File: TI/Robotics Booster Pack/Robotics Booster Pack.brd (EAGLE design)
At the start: 68.6 x 76.2 mm, 119 parts, among them U1 DRV8800, U10 74LVTH125.RGY, U11 SCHA4B0400, U12 BLUETOOTH-RN41", U13 XBEE-1XBEE-1_LOCK, U14 FDMA1024NZ, U2 DRV8800, U3 DRV8800, U4 DRV8800, U5 TPS5331[8/9].DQP, U6 TPS62082.DSG, U7 PCA9557.RGV, U8 MPU-6050, U9 INA220.DGS

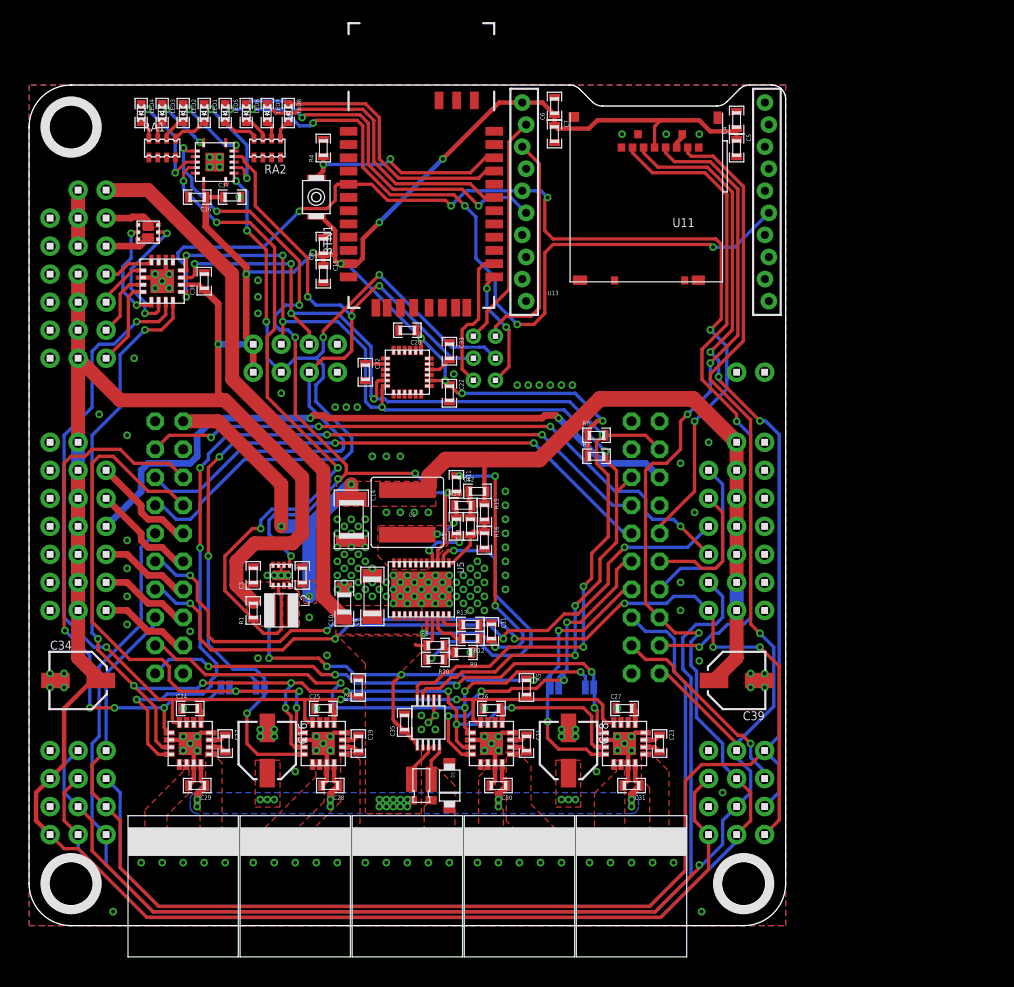
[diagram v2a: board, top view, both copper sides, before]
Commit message: Addressed all issues in github repo Moved GPIO & Mosfet connections up because of USB connector in Launchpad Fixed SPI pin swap Added diode between 5v and VBUS Changed jumpers for UART BT/XBee selection to SMD Jumpers
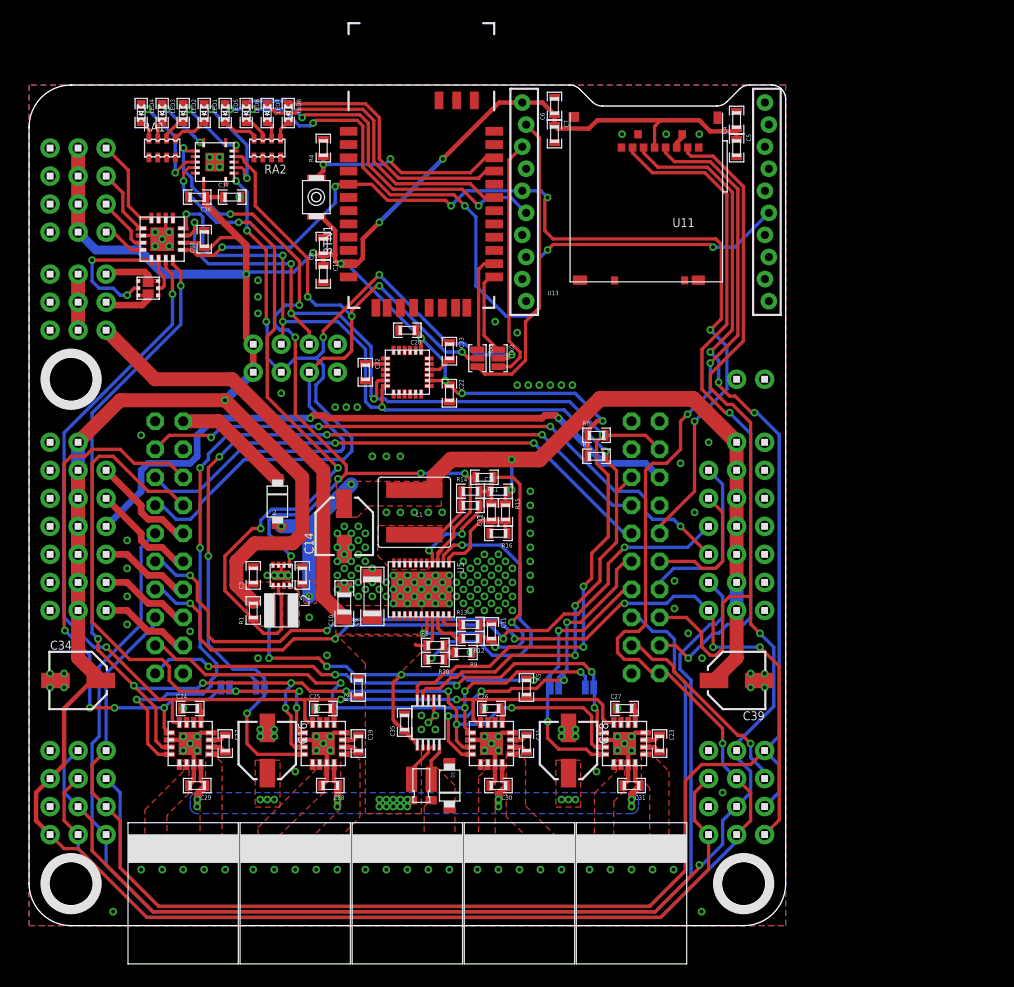
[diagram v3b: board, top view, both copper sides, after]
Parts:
- removed H23: 2X3, headers(2mm):2X3
- removed H27: 1X2, headers(.1in):1X2
- added D2: (no value), nxp:SOD123W
- added RXI, TXO: (no value), solderjumper:3.LRG
- C14: device standardparts:1210 -> microbuilder:PANASONIC_C
- C16, C18: value 100uF -> 47uF
- H7, H8, H9: value 1X2 -> 1X3; device headers(.1in):1X2 -> headers(.1in):1X3
- U14: value FDMA1024NZ -> FDMA3028N
- moved U$11 22.9 mm to (3.81, 49.5)
- moved H10 19.0 mm to (1.91, 70.5), turned to 270 degrees
- moved H11 19.0 mm to (4.45, 70.5), turned to 270 degrees
- moved H12 11.4 mm to (6.99, 70.5)
- moved H8 7.62 mm to (4.45, 54.0)
- moved H9 5.08 mm to (6.99, 59.1)
- moved U14 5.08 mm to (10.8, 57.8)
- moved C38 3.81 mm to (15.9, 62.2)
- moved U7 3.81 mm to (12.1, 62.2)
- moved R11 2.62 mm to (41.3, 40.6), turned to 180 degrees
- moved H7 2.54 mm to (1.91, 59.1), turned to 270 degrees
- moved C1 2.29 mm to (40.0, 38.1), turned to 180 degrees
- moved C13 2.29 mm to (41.9, 37.5)
- moved C12 1.91 mm to (42.5, 39.4)
- moved R15 1.91 mm to (43.2, 37.5)
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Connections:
- new net N$16: D2.P$2, U$8.VBUS
- net 5.0V: now also C14.+, D2.P$1; no longer C14.1, U$8.VBUS
- net BT.RXI: now also RXI.1; no longer H23.5
- net BT.TXO: now also TXO.1; no longer H23.6
- net GND: now also C14.-, H7.3; no longer C14.2
- net SPI.MISO: now also U$8.PA4; no longer U$8.PA2
- net SPI.SCLK: now also U$8.PA2; no longer U$8.PA4
- net UART.RXI: now also RXI.2; no longer H23.3
- net UART.TXO: now also TXO.2; no longer H23.4
- net VBAT: now also H9.3; no longer H27.2
- net VIN: now also H8.3; no longer H27.1
- net XBEE.RXI: now also RXI.3; no longer H23.1
- net XBEE.TXO: now also TXO.3; no longer H23.2
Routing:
- net 5.0V: track 90.8 -> 74.8 mm, vias 3 -> 5
- net VBAT: track 75.5 -> 64.4 mm
- net N$16: track 0.00 -> 10.8 mm
- net FET1.G: track 12.1 -> 3.17 mm, vias 2 -> 0
- net XBEE.RXI: track 21.2 -> 27.5 mm
- net !RST: track 93.8 -> 87.8 mm
- net SPI.MISO: track 156.1 -> 161.1 mm
- net BT.RXI: track 13.0 -> 8.97 mm
- net IO0: track 4.63 -> 8.62 mm
- net IO3: track 7.75 -> 3.85 mm
- net M.EN: track 108.2 -> 111.7 mm
- net 5V.PG: track 72.9 -> 76.3 mm
- net BT.TXO: track 11.0 -> 7.73 mm, vias 2 -> 0
- net I2C.SDA: track 95.4 -> 98.5 mm
- net N$2: track 5.09 -> 8.11 mm
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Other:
- board text added: "!CS!"
- board text added: "VBATT"
- board text removed: "CS"

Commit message: Created AS5035 FLoating Encoder
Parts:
- moved H6 12.7 mm to (6.99, 41.3), turned to 270 degrees
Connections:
- net AD0: now also H6.6; no longer H6.1
- net AD1: now also H6.5; no longer H6.2
- net AD2: now also H6.4; no longer H6.3
- net AD3: now also H6.3; no longer H6.4
- net AD4: now also H6.2; no longer H6.5
- net AD5: now also H6.1; no longer H6.6

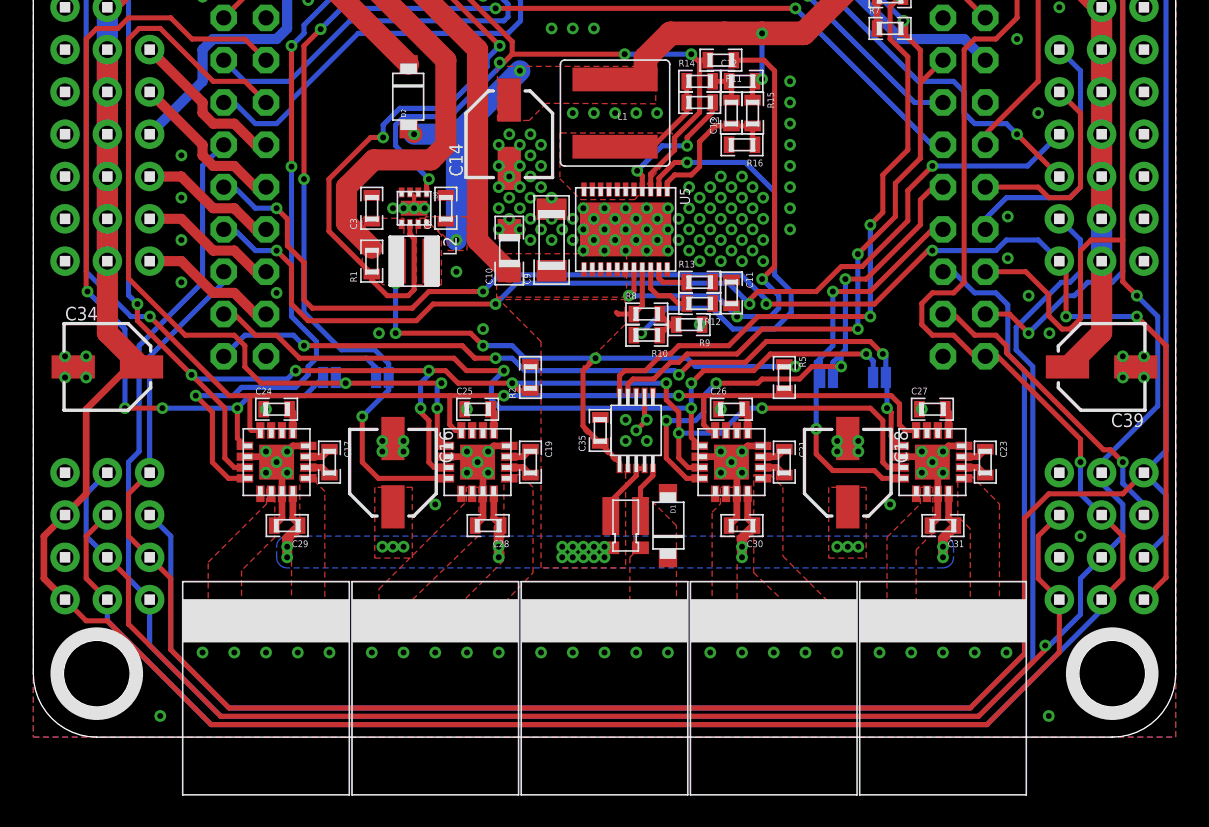
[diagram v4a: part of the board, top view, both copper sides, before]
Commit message: Changed Pinouts of BoosterPack * SPI Encoders replaced with QEI * SD Card/SPI interface moved to port F * Motor Control Signals moved to port A
Layout still needs to be redone...
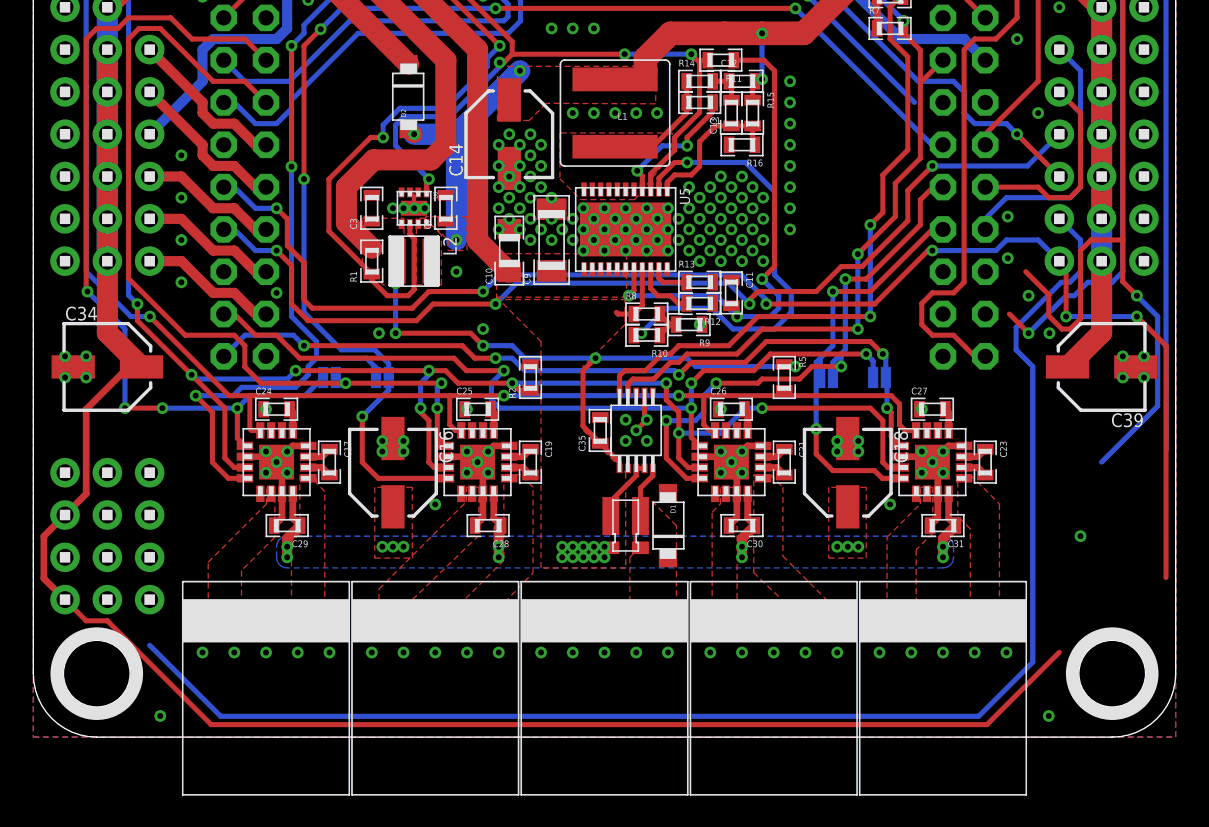
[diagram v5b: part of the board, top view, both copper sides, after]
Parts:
- removed H15, H16: 2X3, headers(.1in):2X3
- moved H14 59.9 mm to (1.91, 8.26)
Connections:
- removed net ENC0.!CS: H13.5, U$8.PD6
- removed net ENC1.!CS: H14.5, U$8.PD7
- removed net SPI.FSS: U$8.PA3, U11.!CS!/NC/DAT3
- new net QEI0.A: U$8.PD6
- new net QEI0.B: U$8.PD7
- new net QEI1.A: U$8.PC5
- new net QEI1.B: U$8.PC6
- new net SPI*.!CS: U$8.PC7
- new net SPI.!CS: U$8.PC4, U11.!CS!/NC/DAT3
- new net UART*.RXI: U$8.PE5
- new net UART*.TXO: U$8.PE4
- net 3.3V: no longer H15.1, H16.1
- net GND: no longer H15.2, H16.2
- net M0.DIR: now also U$8.PA2; no longer U$8.PC4
- net M1.DIR: now also U$8.PA3; no longer U$8.PC5
- net M2.DIR: now also U$8.PA4; no longer U$8.PC6
- net M3.DIR: now also U$8.PA5; no longer U$8.PC7
- net SPI.MISO: now also U$8.PF0; no longer H13.4, H14.4, H15.4, H16.4, U$8.PA4
- net SPI.MOSI: now also U$8.PF1; no longer H13.6, H14.6, H15.6, H16.6, U$8.PA5
- net SPI.SCLK: now also U$8.PF2; no longer H13.3, H14.3, H15.3, H16.3, U$8.PA2
- net SVRO4/ENC2.!CS: no longer H15.5, U$8.PE4
- net SVRO5/ENC3.!CS: no longer H16.5, U$8.PE5
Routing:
- net SPI.MOSI: track 168.0 -> 63.3 mm
- net SPI.SCLK: track 153.1 -> 60.4 mm, vias 3 -> 2
- net ENC0.!CS: track 88.7 -> 0.00 mm
- net SPI.MISO: track 161.1 -> 75.2 mm, vias 2 -> 1
- net SPI.FSS: track 62.2 -> 0.00 mm, vias 2 -> 0
- net SPI.!CS: track 0.00 -> 60.7 mm, vias 0 -> 2
- net SVRO4/ENC2.!CS: track 118.5 -> 85.6 mm
- net ENC1.!CS: track 18.4 -> 0.00 mm, vias 1 -> 0
- net 3.3V: track 363.2 -> 353.9 mm
- net SVRO5/ENC3.!CS: track 85.3 -> 82.8 mm
- net M0.DIR: track 82.3 -> 80.6 mm
- net M1.DIR: track 77.0 -> 76.4 mm
- net M3.DIR: track 25.2 -> 24.5 mm
- net M2.DIR: track 33.2 -> 32.6 mm

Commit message: Started routing v2. And by started, I mean rerouting _everything_
... The heck's wrong with me ...
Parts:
- removed BTN1: B3U-1000P(M)-B, omron:B3U-1000P(M)-B
- removed U$6, U$7: 1X4, headers(.1in):1X4
- added J2: (no value), solderjumper:2.MED
- added U$14: HOLE.4MM, screw_holes:4MM
- added U$9: 2X4, headers(.1in):2X4
- C14, C16, C18, C34, C39: device microbuilder:PANASONIC_C -> microbuilder:PANASONIC_D
- R2, R5: value 100k -> 10k
- RXI, TXO: device solderjumper:3.LRG -> solderjumper:3.LRG.12
- moved H14 59.7 mm to (61.6, 6.99)
- moved H13 6.35 mm to (1.91, 6.99)
- moved C34 5.71 mm to (4.45, 16.5), turned to 270 degrees
- moved C39 5.71 mm to (64.1, 16.5), turned to 270 degrees
- moved L2 5.68 mm to (20.3, 33.7)
- moved R1 5.68 mm to (17.8, 33.7)
- moved C2 5.68 mm to (22.2, 36.8)
- moved C3 5.68 mm to (17.8, 36.8)
- moved U6 5.68 mm to (20.3, 36.8)
- moved U$11 5.12 mm to (3.17, 44.5)
- moved H1 4.45 mm to (66.7, 24.1)
- moved H2 4.45 mm to (64.1, 24.1)
- moved H22 4.45 mm to (64.1, 39.4)
- moved H26 4.45 mm to (4.45, 39.4)
- moved H3 4.45 mm to (61.6, 36.8)
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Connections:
- removed net N$43: LED2.P$1, U10.6
- removed net N$51: LED1.P$2, RA1.8
- removed net N$52: LED2.P$2, RA1.6
- removed net N$6 (its old number): LED1.P$1, U10.3
- removed net SPI*.!CS: U$8.PC7
- removed net SVRO4/ENC2.!CS: H3.5
- removed net SVRO5/ENC3.!CS: H3.6
- removed net UART*.RXI: U$8.PE5
- removed net UART*.TXO: U$8.PE4
- new net N$26: LED2.P$2, U10.6
- new net N$28: LED1.P$2, U10.3
- new net N$30: LED1.P$1, RA1.8
- new net N$31: LED2.P$1, RA1.6
- new net SVRO4: H3.5, U$8.PE4
- new net SVRO5: H3.6, U$8.PE5
- net 3.3V: now also H13.3, H14.3, J2.2, U$9.1, U$9.2; no longer BTN1.2, H13.1, H14.1, U$6.1, U$7.1
- net 5.0V: no longer C2.1, U6.8
- net BT.RESET: now also J2.1; no longer BTN1.1
- net GND: now also H13.1, H14.1, U$9.7, U$9.8; no longer H13.2, H14.2, U$6.4, U$7.4
- net I2C.SCL: now also U$9.5, U$9.6; no longer U$6.3
- net I2C.SDA: now also U$9.3, U$9.4; no longer U$6.2
- net M.MODE: no longer U7.11
- net M0.DIR: now also U$8.PC4; no longer U$8.PA2
- net M1.DIR: now also U$8.PC7; no longer U$8.PA3
- net M2.DIR: now also U$8.PF0; no longer U$8.PA4
- net M3.DIR: now also U$8.PF4; no longer U$8.PA5
- net N$16: now also H8.1, H8.2, H8.3; no longer D2.P$2, U$8.VBUS
- net QEI0.A: now also H13.5
- net QEI0.B: now also H13.6
- net QEI1.A: now also H14.5
- net QEI1.B: now also H14.6
- net SPI.!CS: now also U$8.PA3; no longer U$8.PC4
- net SPI.MISO: now also U$8.PA4; no longer U$8.PF0
- net SPI.MOSI: now also U$8.PA5; no longer U$8.PF1
- net SPI.SCLK: now also U$8.PA2; no longer U$8.PF2
- net UART.RXI: no longer U$7.3
- net UART.TXO: no longer U$7.2
- net VIN: now also C2.1, D2.P$2, U$8.VBUS, U6.8; no longer H8.1, H8.2, H8.3
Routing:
- net M.EN: track 111.7 -> 0.00 mm, vias 10 -> 0
- net M.MODE: track 99.5 -> 0.00 mm, vias 4 -> 0
- net 3.3V: track 353.9 -> 259.0 mm, vias 15 -> 7
- net SVRO4/ENC2.!CS: track 85.6 -> 0.00 mm
- net SVRO5/ENC3.!CS: track 82.8 -> 0.00 mm, vias 6 -> 0
- net M0.DIR: track 80.6 -> 0.00 mm, vias 5 -> 0
- net M1.DIR: track 76.4 -> 0.00 mm, vias 5 -> 0
- net XBEE.ASSOCIATE: track 68.3 -> 0.00 mm, vias 5 -> 0
- net SVRO2: track 60.7 -> 0.00 mm, vias 4 -> 0
- net 5V.PG: track 76.3 -> 16.7 mm, vias 8 -> 1
- net AD3: track 59.1 -> 0.00 mm, vias 2 -> 0
- net SVRO3: track 57.1 -> 0.00 mm, vias 4 -> 0
- net QEI0.B: track 0.00 -> 55.8 mm
- net 3.3V.PG: track 64.7 -> 12.1 mm, vias 4 -> 1
- net M1.SPD: track 51.7 -> 0.00 mm, vias 3 -> 0
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- removed copper zone on layer 1, net 3.3V
- removed copper zone on layer 1, net M0+
- removed copper zone on layer 1, net M0-
- removed copper zone on layer 1, net M1+
- removed copper zone on layer 1, net M1-
- removed copper zone on layer 1, net M2+
- removed copper zone on layer 1, net M2-
- removed copper zone on layer 1, net M3-
- removed copper zone on layer 1, net N$12
- removed copper zone on layer 16, net VBAT
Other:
- board text added: "!RST"
- board text added: "ENC 0"
- board text added: "ENC 1"
- board text added: "FET"
- board text removed: "!CS!"
- board text removed: "ENC 0|2"
- board text removed: "ENC 1|3"
- board text removed: "Factory RST"
- board text removed: "MISO"
- board text removed: "MOSI"
- board text removed: "RST"
- board text removed: "SCLK"
- board text removed: "UART"
- board text removed: "VBATT"
